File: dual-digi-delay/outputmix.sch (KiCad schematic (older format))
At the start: 15 parts, among them U1 TL072

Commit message: Final revision of dual digi delay
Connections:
- net DELAY1_WET renamed DELAY1_WET_LEVEL
- net DELAY2_WET renamed DELAY2_WET_LEVEL
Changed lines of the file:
@@
 $Descr A4 11693 8268
 encoding utf-8
-Sheet 9 10
+Sheet 10 10
 Title ""
 Date ""
@@
 	2600 4300 2750 4300
 Text HLabel 2600 3350 0    50   Input ~ 0
-DELAY2_WET
+DELAY2_WET_LEVEL
 Text HLabel 2600 4300 0    50   Input ~ 0
-DELAY1_WET
+DELAY1_WET_LEVEL
 Text HLabel 4300 4650 3    50   Input ~ 0
 DELAY_MIX

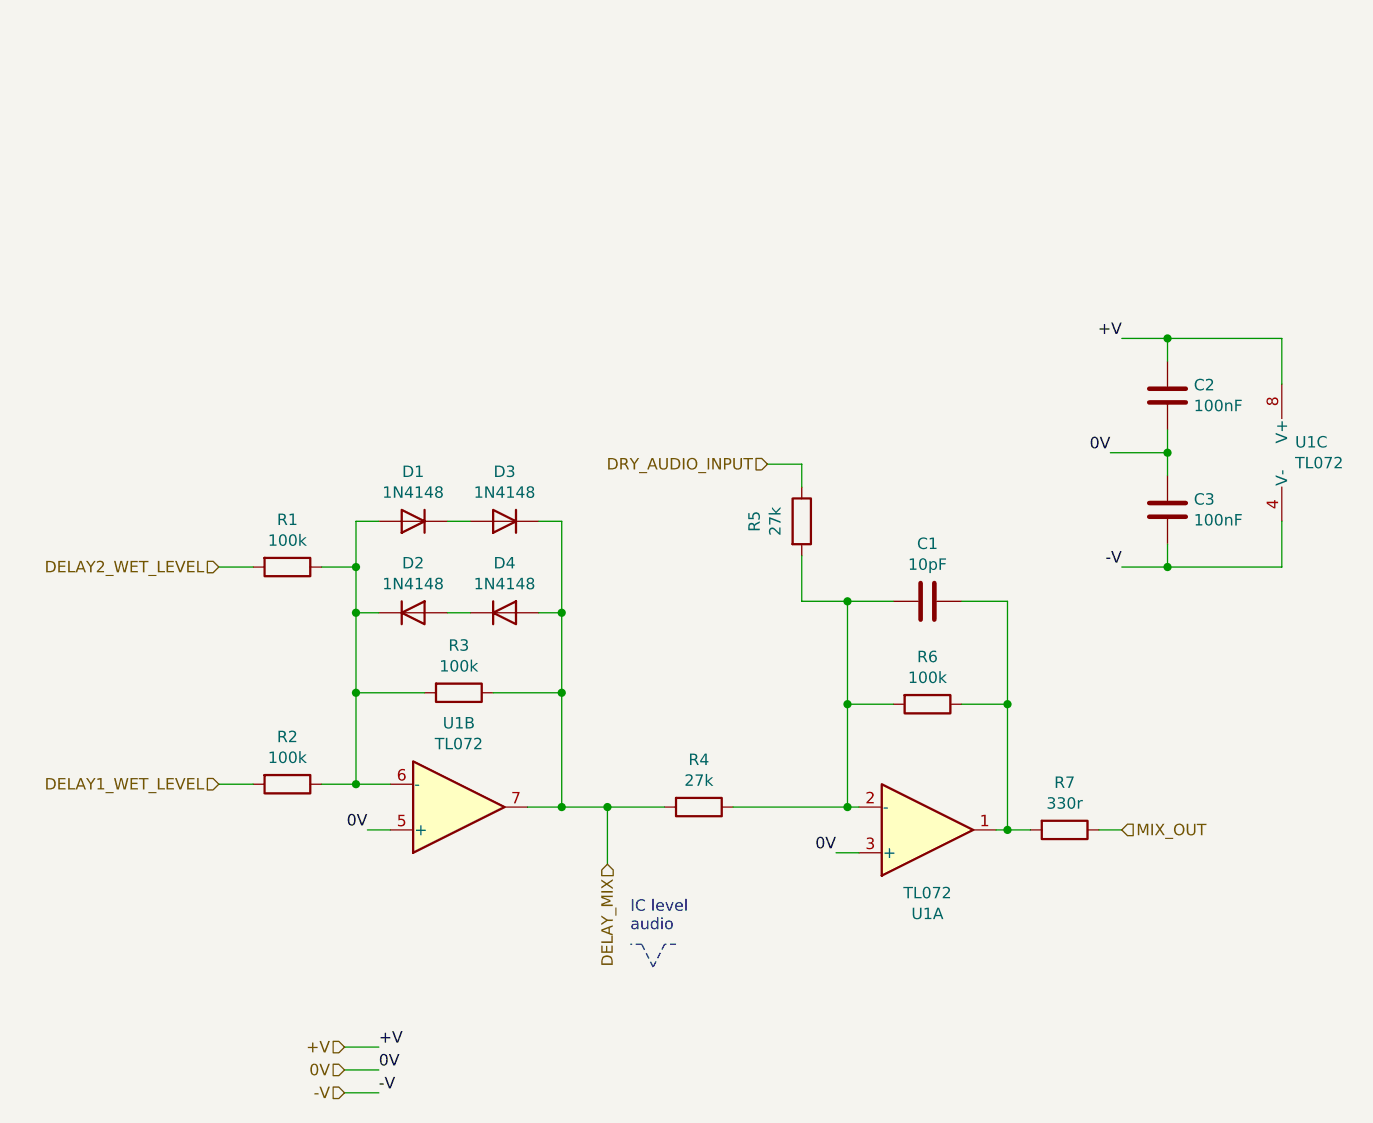
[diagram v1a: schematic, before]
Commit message: Updating digi delay to rev 2
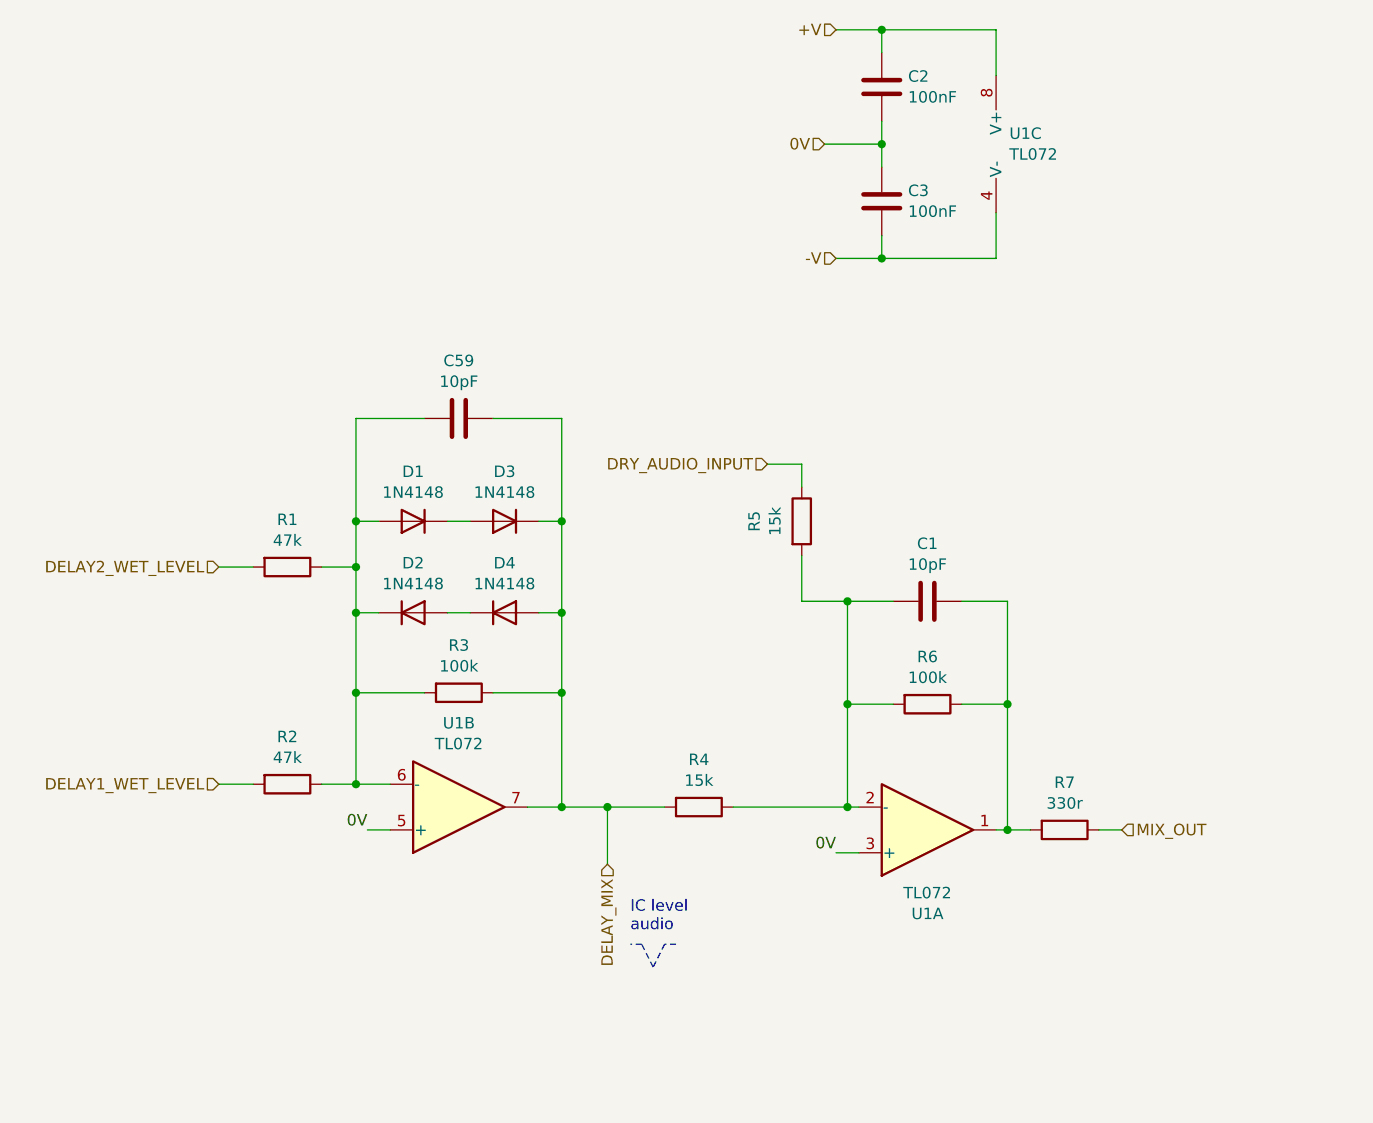
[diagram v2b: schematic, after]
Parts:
- added C59: 10pF, rumblesan-footprints:C_Rect_L7.0mm_W3.5mm_P5.00mm, symbol Device:C
- R1, R2: value 100k -> 47k
- R4, R5: value 27k -> 15k
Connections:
- net DELAY_MIX: now also C59.1
- net at D1.2 (A), D2.1 (K), R1.1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: now also C59.2
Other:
- moved on the sheet: C2, C3, U1C
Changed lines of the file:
@@
 $Descr A4 11693 8268
 encoding utf-8
-Sheet 10 10
+Sheet 11 11
 Title ""
 Date ""
@@
 AR Path="/62AB7D6F/62AEDF6D" Ref="R4"  Part="1"
 F 0 "R4" V 4493 4400 50  0000 C CNN
-F 1 "27k" V 4584 4400 50  0000 C CNN
+F 1 "15k" V 4584 4400 50  0000 C CNN
 F 2 "rumblesan-footprints:Resistor_THT_L6.3mm_D2.5mm_P10.16mm_Horizontal" V 4630 4400 50  0001 C CNN
 F 3 "~" H 4700 4400 50  0001 C CNN
@@
 AR Path="/62AB7D6F/62AEDFF4" Ref="R1"  Part="1"
 F 0 "R1" V 2693 3350 50  0000 C CNN
-F 1 "100k" V 2784 3350 50  0000 C CNN
+F 1 "47k" V 2784 3350 50  0000 C CNN
 F 2 "rumblesan-footprints:Resistor_THT_L6.3mm_D2.5mm_P10.16mm_Horizontal" V 2830 3350 50  0001 C CNN
 F 3 "~" H 2900 3350 50  0001 C CNN
@@
 AR Path="/62AB7D6F/62AEDFFA" Ref="R2"  Part="1"
 F 0 "R2" V 2693 4300 50  0000 C CNN
-F 1 "100k" V 2784 4300 50  0000 C CNN
+F 1 "47k" V 2784 4300 50  0000 C CNN
 F 2 "rumblesan-footprints:Resistor_THT_L6.3mm_D2.5mm_P10.16mm_Horizontal" V 2830 4300 50  0001 C CNN
 F 3 "~" H 2900 4300 50  0001 C CNN
@@
 AR Path="/62AB7D6F/62AEDF96" Ref="R5"  Part="1"
 F 0 "R5" V 4943 3150 50  0000 C CNN
-F 1 "27k" V 5034 3150 50  0000 C CNN
+F 1 "15k" V 5034 3150 50  0000 C CNN
 F 2 "rumblesan-footprints:Resistor_THT_L6.3mm_D2.5mm_P10.16mm_Horizontal" V 5080 3150 50  0001 C CNN
 F 3 "~" H 5150 3150 50  0001 C CNN
@@
 L Device:C C?
 U 1 1 62BCD8B9
-P 6750 2600
+P 5500 1250
 AR Path="/62BCD8B9" Ref="C?"  Part="1"
 AR Path="/62AB7D6F/62BCD8B9" Ref="C2"  Part="1"
-F 0 "C2" H 6635 2554 50  0000 R CNN
-F 1 "100nF" H 6635 2645 50  0000 R CNN
-F 2 "rumblesan-footprints:C_Rect_L7.0mm_W3.5mm_P5.00mm" H 6788 2450 50  0001 C CNN
-F 3 "~" H 6750 2600 50  0001 C CNN
-	1    6750 2600
+F 0 "C2" H 5385 1204 50  0000 R CNN
+F 1 "100nF" H 5385 1295 50  0000 R CNN
+F 2 "rumblesan-footprints:C_Rect_L7.0mm_W3.5mm_P5.00mm" H 5538 1100 50  0001 C CNN
+F 3 "~" H 5500 1250 50  0001 C CNN
+	1    5500 1250
 	-1   0    0    1
 $EndComp
 Wire Wire Line
-	6750 2350 6750 2450
-Wire Wire Line
-	6750 2850 6750 2750
-Connection ~ 6750 2850
+	5500 1000 5500 1100
+Wire Wire Line
+	5500 1500 5500 1400
+Connection ~ 5500 1500
 $Comp
 L Device:C C?
 U 1 1 62BCD8C2
-P 6750 3100
+P 5500 1750
 AR Path="/62BCD8C2" Ref="C?"  Part="1"
 AR Path="/62AB7D6F/62BCD8C2" Ref="C3"  Part="1"
-F 0 "C3" H 6635 3054 50  0000 R CNN
-F 1 "100nF" H 6635 3145 50  0000 R CNN
-F 2 "rumblesan-footprints:C_Rect_L7.0mm_W3.5mm_P5.00mm" H 6788 2950 50  0001 C CNN
-F 3 "~" H 6750 3100 50  0001 C CNN
-	1    6750 3100
+F 0 "C3" H 5385 1704 50  0000 R CNN
+F 1 "100nF" H 5385 1795 50  0000 R CNN
+F 2 "rumblesan-footprints:C_Rect_L7.0mm_W3.5mm_P5.00mm" H 5538 1600 50  0001 C CNN
+F 3 "~" H 5500 1750 50  0001 C CNN
+	1    5500 1750
 	-1   0    0    1
 $EndComp
 Wire Wire Line
-	6750 2950 6750 2850
-Wire Wire Line
-	6750 3350 6750 3250
-Wire Wire Line
-	6550 2350 6750 2350
-Wire Wire Line
-	6550 3350 6750 3350
-Wire Wire Line
-	6500 2850 6750 2850
+	5500 1600 5500 1500
+Wire Wire Line
+	5500 2000 5500 1900
+Wire Wire Line
+	5300 1000 5500 1000
+Wire Wire Line
+	5300 2000 5500 2000
+Wire Wire Line
+	5250 1500 5500 1500
 $Comp
 L Amplifier_Operational:TL072 U?
 U 3 1 62BCD8E2
-P 7350 2850
+P 6100 1500
 AR Path="/62BCD8E2" Ref="U?"  Part="3"
 AR Path="/62AB7D6F/62BCD8E2" Ref="U1"  Part="3"
-F 0 "U1" H 7308 2896 50  0000 L CNN
-F 1 "TL072" H 7308 2805 50  0000 L CNN
-F 2 "rumblesan-footprints:DIP-8_W7.62mm_Socket" H 7350 2850 50  0001 C CNN
-F 3 "http://www.ti.com/lit/ds/symlink/tl071.pdf" H 7350 2850 50  0001 C CNN
-	3    7350 2850
+F 0 "U1" H 6058 1546 50  0000 L CNN
+F 1 "TL072" H 6058 1455 50  0000 L CNN
+F 2 "rumblesan-footprints:DIP-8_W7.62mm_Socket" H 6100 1500 50  0001 C CNN
+F 3 "http://www.ti.com/lit/ds/symlink/tl071.pdf" H 6100 1500 50  0001 C CNN
+	3    6100 1500
 	1    0    0    -1
 $EndComp
 Wire Wire Line
-	6750 2350 7250 2350
-Wire Wire Line
-	7250 2350 7250 2550
-Connection ~ 6750 2350
-Wire Wire Line
-	6750 3350 7250 3350
-Wire Wire Line
-	7250 3150 7250 3350
-Connection ~ 6750 3350
-Text Label 6500 2850 2    50   ~ 0
+	5500 1000 6000 1000
+Wire Wire Line
+	6000 1000 6000 1200
+Connection ~ 5500 1000
+Wire Wire Line
+	5500 2000 6000 2000
+Wire Wire Line
+	6000 1800 6000 2000
+Connection ~ 5500 2000
+Text HLabel 5300 1000 0    50   Input ~ 0
++V
+Text HLabel 5250 1500 0    50   Input ~ 0
 0V
-Text Label 6550 2350 2    50   ~ 0
-+V
-Text Label 6550 3350 2    50   ~ 0
+Text HLabel 5300 2000 0    50   Input ~ 0
 -V
-Text HLabel 3150 5450 0    50   Input ~ 0
-+V
-Text HLabel 3150 5550 0    50   Input ~ 0
-0V
-Text HLabel 3150 5650 0    50   Input ~ 0
--V
-Text Label 3300 5550 0    50   ~ 0
-0V
-Text Label 3300 5450 0    50   ~ 0
-+V
-Text Label 3300 5650 0    50   ~ 0
--V
-Wire Wire Line
-	3150 5450 3300 5450
-Wire Wire Line
-	3150 5550 3300 5550
-Wire Wire Line
-	3300 5650 3150 5650
 Wire Wire Line
 	5150 2900 5150 3000
 Wire Wire Line
 	5150 3300 5150 3500
+$Comp
+L Device:C C?
+U 1 1 61AD7078
+P 3650 2700
+AR Path="/61AD7078" Ref="C?"  Part="1"
+AR Path="/62AB7D6F/61AD7078" Ref="C59"  Part="1"
+F 0 "C59" V 3398 2700 50  0000 C CNN
+F 1 "10pF" V 3489 2700 50  0000 C CNN
+F 2 "rumblesan-footprints:C_Rect_L7.0mm_W3.5mm_P5.00mm" H 3688 2550 50  0001 C CNN
+F 3 "~" H 3650 2700 50  0001 C CNN
+	1    3650 2700
+	0    1    1    0
+$EndComp
+Wire Wire Line
+	3500 2700 3200 2700
+Wire Wire Line
+	3200 2700 3200 3150
+Connection ~ 3200 3150
+Wire Wire Line
+	3800 2700 4100 2700
+Wire Wire Line
+	4100 2700 4100 3150
+Connection ~ 4100 3150
 $EndSCHEMATC
